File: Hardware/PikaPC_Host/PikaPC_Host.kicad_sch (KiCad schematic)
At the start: 0 parts

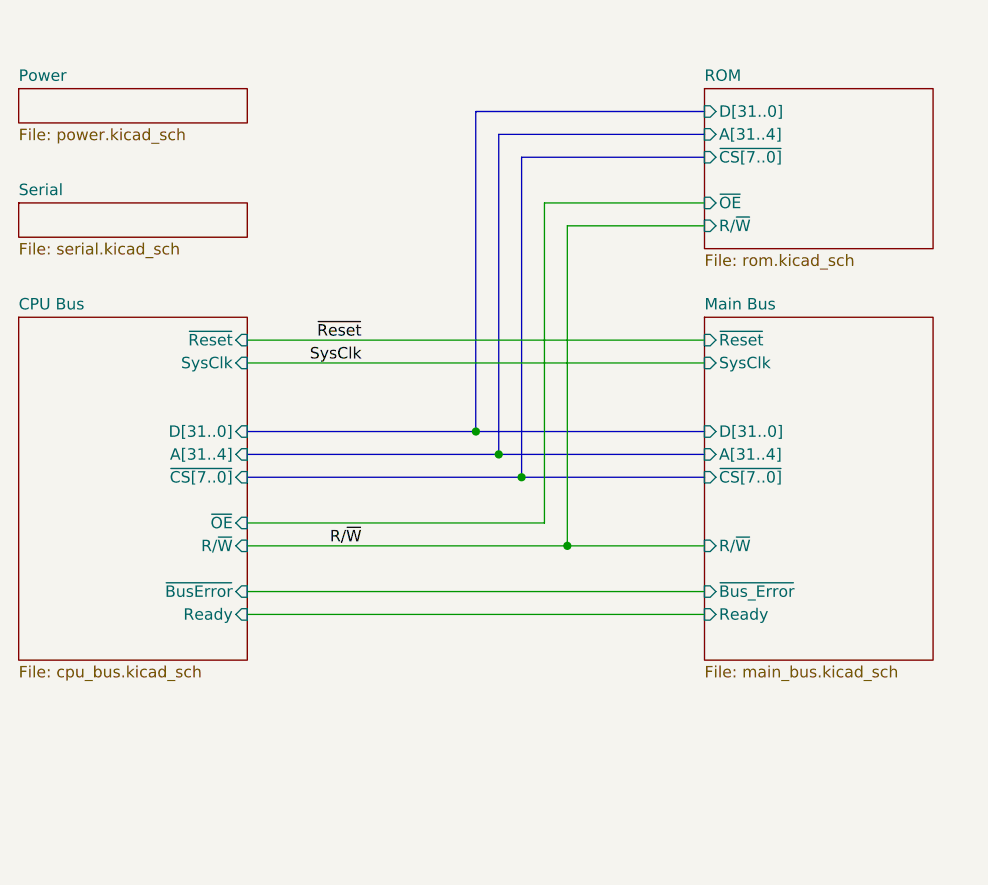
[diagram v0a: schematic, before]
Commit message: Rework bus pinout
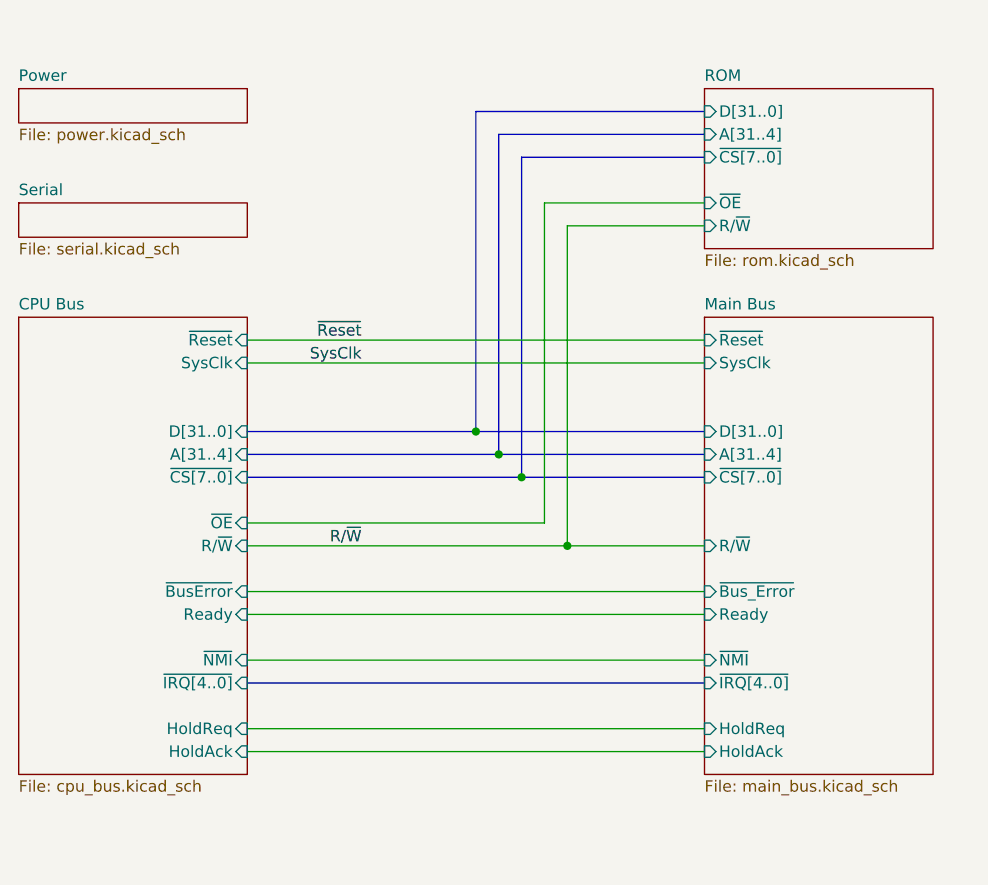
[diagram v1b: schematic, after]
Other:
- sheet CPU Bus ports: added HoldAck, HoldReq, ~{IRQ[4..0]}, ~{NMI}; removed none
- sheet Main Bus ports: added HoldAck, HoldReq, ~{IRQ[4..0]}, ~{NMI}; removed none
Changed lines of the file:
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@@
+	(wire
+		(pts
+			(xy 50.8 88.9) (xy 101.6 88.9)
+		)
+		(stroke
+			(width 0)
+			(type default)
+		)
+	)
 	(wire
 		(pts
@@
 		)
 	)
+	(wire
+		(pts
+			(xy 50.8 96.52) (xy 101.6 96.52)
+		)
+		(stroke
+			(width 0)
+			(type default)
+		)
+	)
 	(bus
 		(pts
@@
 	(bus
 		(pts
+			(xy 50.8 91.44) (xy 101.6 91.44)
+		)
+		(stroke
+			(width 0)
+			(type default)
+		)
+	)
+	(bus
+		(pts
 			(xy 76.2 63.5) (xy 101.6 63.5)
 		)
@@
 		(pts
 			(xy 50.8 83.82) (xy 101.6 83.82)
+		)
+		(stroke
+			(width 0)
+			(type default)
+		)
+	)
+	(wire
+		(pts
+			(xy 50.8 99.06) (xy 101.6 99.06)
 		)
 		(stroke
@@
 	(sheet
 		(at 25.4 50.8)
-		(size 25.4 38.1)
+		(size 25.4 50.8)
 		(exclude_from_sim no)
 		(in_bom yes)
@@
 		)
 		(property "Sheetfile" "cpu_bus.kicad_sch"
-			(at 25.4 89.4846 0)
+			(at 25.4 102.1846 0)
 			(effects
 				(font
@@
 		(pin "~{OE}" input
 			(at 50.8 73.66 0)
+			(effects
+				(font
+					(size 1.27 1.27)
+				)
+				(justify right)
+			)
+		)
+		(pin "~{NMI}" input
+			(at 50.8 88.9 0)
+			(effects
+				(font
+					(size 1.27 1.27)
+				)
+				(justify right)
+			)
+		)
+		(pin "~{IRQ[4..0]}" input
+			(at 50.8 91.44 0)
+			(effects
+				(font
+					(size 1.27 1.27)
+				)
+				(justify right)
+			)
+		)
+		(pin "HoldReq" input
+			(at 50.8 96.52 0)
+			(effects
+				(font
+					(size 1.27 1.27)
+				)
+				(justify right)
+			)
+		)
+		(pin "HoldAck" input
+			(at 50.8 99.06 0)
 			(effects
 				(font
@@
 	(sheet
 		(at 101.6 50.8)
-		(size 25.4 38.1)
+		(size 25.4 50.8)
 		(exclude_from_sim no)
 		(in_bom yes)
@@
 		)
 		(property "Sheetfile" "main_bus.kicad_sch"
-			(at 101.6 89.4846 0)
+			(at 101.6 102.1846 0)
 			(effects
 				(font
@@
 			(effects
 				(font
+					(size 1.27 1.27)
+				)
+				(justify left)
+			)
+		)
+		(pin "HoldReq" input
+			(at 101.6 96.52 180)
+			(effects
+				(font
+					(size 1.27 1.27)
+				)
+				(justify left)
+			)
+		)
+		(pin "HoldAck" input
+			(at 101.6 99.06 180)
+			(effects
+				(font
+					(size 1.27 1.27)
+				)
+				(justify left)
+			)
+		)
+		(pin "~{NMI}" input
+			(at 101.6 88.9 180)
+			(effects
+				(font
+					(size 1.27 1.27)
+				)
+				(justify left)
+			)
+		)
+		(pin "~{IRQ[4..0]}" input
+			(at 101.6 91.44 180)
+			(effects
+				(font

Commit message: Host Card refinement
add main bus clock selection
silkscreen cleanup
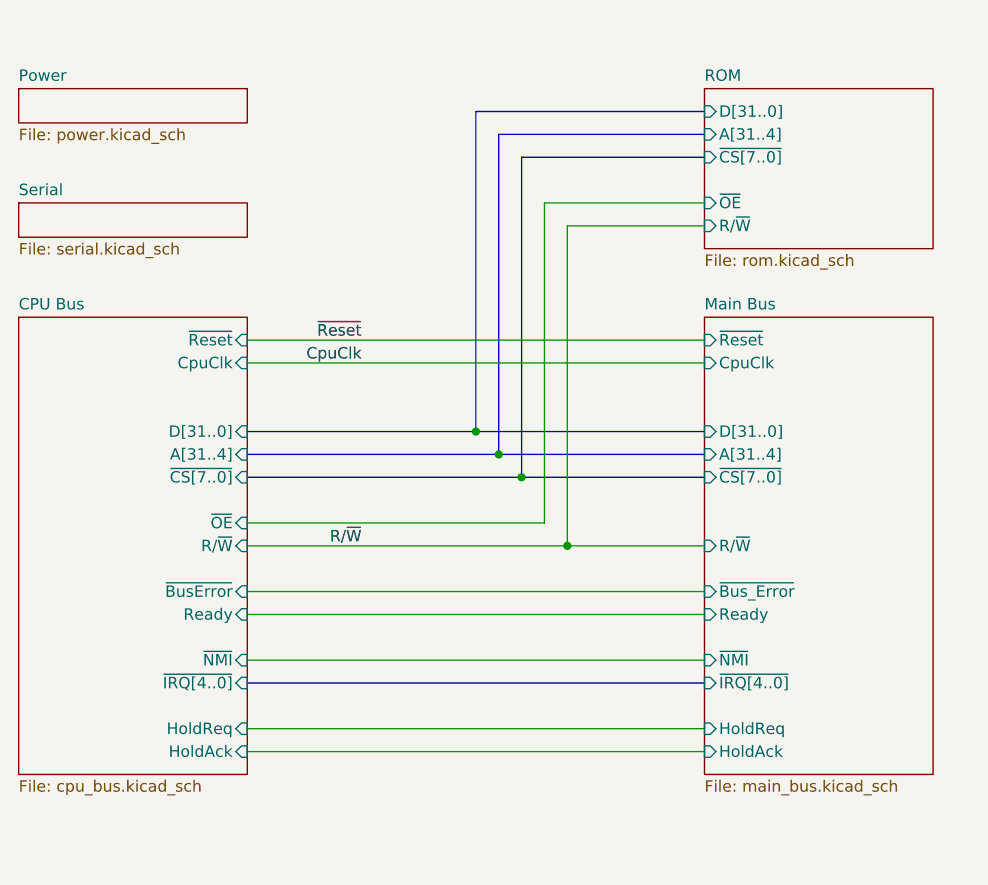
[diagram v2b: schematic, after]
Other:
- sheet CPU Bus ports: added CpuClk; removed SysClk
- sheet Main Bus ports: added CpuClk; removed SysClk
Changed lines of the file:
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@@
 		)
 	)
-	(label "SysClk"
+	(label "CpuClk"
 		(at 63.5 55.88 180)
 		(effects
@@
 			)
 		)
-		(pin "SysClk" input
+		(pin "CpuClk" input
 			(at 50.8 55.88 0)
 			(effects
@@
 			)
 		)
-		(pin "SysClk" input
+		(pin "CpuClk" input
 			(at 101.6 55.88 180)
 			(effects

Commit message: Host Card updates
- add missing bus pull-ups
- add on-board DRAM
- add series termination resistors to AD bus
- fix DE9 footprint mounting hole location
- fix double-buffered bus clock
- use 74'2244 buffer w/series term resistors for bus control signals
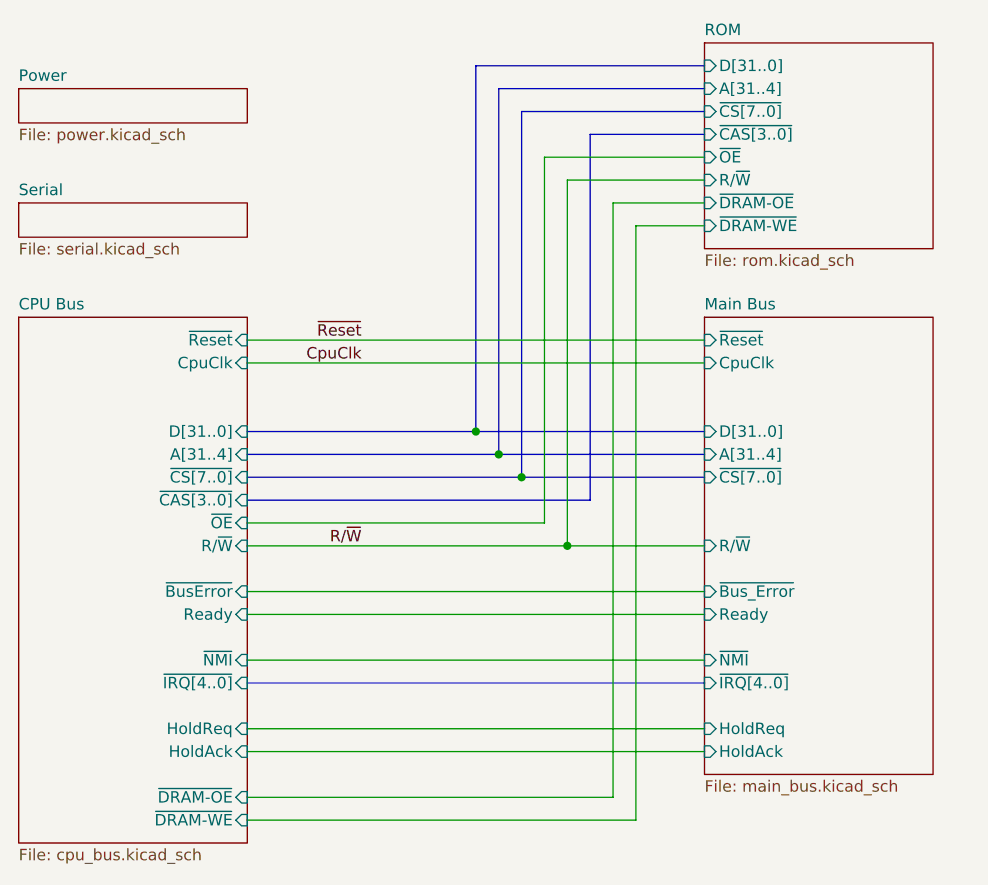
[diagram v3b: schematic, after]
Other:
- sheet CPU Bus ports: added ~{CAS[3..0]}, ~{DRAM-OE}, ~{DRAM-WE}; removed none
- sheet ROM ports: added ~{CAS[3..0]}, ~{DRAM-OE}, ~{DRAM-WE}; removed none
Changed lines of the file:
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@@
+	(bus
+		(pts
+			(xy 50.8 71.12) (xy 88.9 71.12)
+		)
+		(stroke
+			(width 0)
+			(type default)
+		)
+	)
 	(bus
 		(pts
@@
 	(bus
 		(pts
-			(xy 101.6 27.94) (xy 76.2 27.94)
+			(xy 88.9 30.48) (xy 101.6 30.48)
+		)
+		(stroke
+			(width 0)
+			(type default)
+		)
+	)
+	(bus
+		(pts
+			(xy 101.6 22.86) (xy 76.2 22.86)
 		)
 		(stroke
@@
 	(wire
 		(pts
-			(xy 101.6 40.64) (xy 86.36 40.64)
-		)
-		(stroke
-			(width 0)
-			(type default)
-		)
-	)
-	(bus
-		(pts
-			(xy 101.6 30.48) (xy 78.74 30.48)
+			(xy 101.6 35.56) (xy 86.36 35.56)
+		)
+		(stroke
+			(width 0)
+			(type default)
+		)
+	)
+	(bus
+		(pts
+			(xy 101.6 25.4) (xy 78.74 25.4)
 		)
 		(stroke
@@
 	(wire
 		(pts
+			(xy 50.8 106.68) (xy 93.98 106.68)
+		)
+		(stroke
+			(width 0)
+			(type default)
+		)
+	)
+	(wire
+		(pts
 			(xy 50.8 55.88) (xy 101.6 55.88)
 		)
@@
 	(wire
 		(pts
-			(xy 101.6 38.1) (xy 83.82 38.1)
-		)
-		(stroke
-			(width 0)
-			(type default)
-		)
-	)
-	(bus
-		(pts
-			(xy 81.28 33.02) (xy 81.28 68.58)
+			(xy 93.98 106.68) (xy 93.98 40.64)
+		)
+		(stroke
+			(width 0)
+			(type default)
+		)
+	)
+	(wire
+		(pts
+			(xy 101.6 33.02) (xy 83.82 33.02)
+		)
+		(stroke
+			(width 0)
+			(type default)
+		)
+	)
+	(bus
+		(pts
+			(xy 81.28 27.94) (xy 81.28 68.58)
 		)
 		(stroke
@@
 	(bus
 		(pts
-			(xy 76.2 27.94) (xy 76.2 63.5)
+			(xy 76.2 22.86) (xy 76.2 63.5)
 		)
 		(stroke
@@
 	(bus
 		(pts
-			(xy 78.74 30.48) (xy 78.74 66.04)
+			(xy 78.74 25.4) (xy 78.74 66.04)
 		)
 		(stroke
@@
 	(wire
 		(pts
+			(xy 91.44 104.14) (xy 50.8 104.14)
+		)
+		(stroke
+			(width 0)
+			(type default)
+		)
+	)
+	(bus
+		(pts
+			(xy 88.9 71.12) (xy 88.9 30.48)
+		)
+		(stroke
+			(width 0)
+			(type default)
+		)
+	)
+	(wire
+		(pts
+			(xy 91.44 38.1) (xy 91.44 104.14)
+		)
+		(stroke
+			(width 0)
+			(type default)
+		)
+	)
+	(wire
+		(pts
 			(xy 50.8 73.66) (xy 83.82 73.66)
 		)
@@
 	(wire
 		(pts
-			(xy 86.36 40.64) (xy 86.36 76.2)
+			(xy 86.36 35.56) (xy 86.36 76.2)
 		)
 		(stroke
@@
 	(wire
 		(pts
-			(xy 83.82 38.1) (xy 83.82 73.66)
-		)
-		(stroke
-			(width 0)
-			(type default)
-		)
-	)
-	(bus
-		(pts
-			(xy 101.6 33.02) (xy 81.28 33.02)
+			(xy 83.82 33.02) (xy 83.82 73.66)
+		)
+		(stroke
+			(width 0)
+			(type default)
+		)
+	)
+	(wire
+		(pts
+			(xy 101.6 38.1) (xy 91.44 38.1)
+		)
+		(stroke
+			(width 0)
+			(type default)
+		)
+	)
+	(wire
+		(pts
+			(xy 93.98 40.64) (xy 101.6 40.64)
+		)
+		(stroke
+			(width 0)
+			(type default)
+		)
+	)
+	(bus
+		(pts
+			(xy 101.6 27.94) (xy 81.28 27.94)
 		)
 		(stroke
@@
 	)
 	(sheet
-		(at 101.6 25.4)
-		(size 25.4 17.78)
+		(at 101.6 20.32)
+		(size 25.4 22.86)
 		(exclude_from_sim no)
 		(in_bom yes)
@@
 		)
 		(property "Sheetname" "ROM"
-			(at 101.6 24.6884 0)
+			(at 101.6 19.6084 0)
 			(effects
 				(font
@@
 		)
 		(pin "R{slash}~{W}" input
+			(at 101.6 35.56 180)
+			(effects
+				(font
+					(size 1.27 1.27)
+				)
+				(justify left)
+			)
+		)
+		(pin "~{CS[7..0]}" input
+			(at 101.6 27.94 180)
+			(effects
+				(font
+					(size 1.27 1.27)
+				)
+				(justify left)
+			)
+		)
+		(pin "~{OE}" input
+			(at 101.6 33.02 180)
+			(effects
+				(font
+					(size 1.27 1.27)
+				)
+				(justify left)
+			)
+		)
+		(pin "D[31..0]" input
+			(at 101.6 22.86 180)
+			(effects
+				(font
+					(size 1.27 1.27)
+				)
+				(justify left)
+			)
+		)
+		(pin "A[31..4]" input
+			(at 101.6 25.4 180)
+			(effects
+				(font
+					(size 1.27 1.27)
+				)
+				(justify left)
+			)
+		)
+		(pin "~{CAS[3..0]}" input
+			(at 101.6 30.48 180)
+			(effects
+				(font
+					(size 1.27 1.27)
+				)
+				(justify left)
+			)
+		)
+		(pin "~{DRAM-OE}" input
+			(at 101.6 38.1 180)
+			(effects
+				(font
+					(size 1.27 1.27)
+				)
+				(justify left)
+			)
+		)
+		(pin "~{DRAM-WE}" input
 			(at 101.6 40.64 180)
-			(effects
-				(font
-					(size 1.27 1.27)
-				)
-				(justify left)
-			)
-		)
-		(pin "~{CS[7..0]}" input
-			(at 101.6 33.02 180)
-			(effects
-				(font
-					(size 1.27 1.27)
-				)
-				(justify left)
-			)
-		)
-		(pin "~{OE}" input
-			(at 101.6 38.1 180)
-			(effects
-				(font
-					(size 1.27 1.27)
-				)
-				(justify left)
-			)
-		)
-		(pin "D[31..0]" input
-			(at 101.6 27.94 180)
-			(effects
-				(font
-					(size 1.27 1.27)
-				)
-				(justify left)
-			)
-		)
-		(pin "A[31..4]" input
-			(at 101.6 30.48 180)
 			(effects
 				(font
@@
 	(sheet
 		(at 25.4 50.8)
-		(size 25.4 50.8)
+		(size 25.4 58.42)
 		(exclude_from_sim no)
 		(in_bom yes)
@@
 		)
 		(property "Sheetfile" "cpu_bus.kicad_sch"
-			(at 25.4 102.1846 0)
+			(at 25.4 109.8046 0)
 			(effects
 				(font
@@
 			(effects
 				(font
+					(size 1.27 1.27)
+				)
+				(justify right)
+			)
+		)
+		(pin "~{CAS[3..0]}" input
+			(at 50.8 71.12 0)
+			(effects
+				(font
+					(size 1.27 1.27)
+				)
+				(justify right)
+			)
+		)
+		(pin "~{DRAM-OE}" input
+			(at 50.8 104.14 0)
+			(effects
+				(font
+					(size 1.27 1.27)
+				)
+				(justify right)
+			)
+		)
+		(pin "~{DRAM-WE}" input
+			(at 50.8 106.68 0)
+			(effects
+				(font
